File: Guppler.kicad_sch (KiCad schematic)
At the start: 21 parts, among them Q1 AO3400A, Q2 AO3400A, Q3 AO3400A, SW1 SW_Push, SW2 SW_Push, U1 LM2596S-3.3, U2 ESP32-C3-WROOM-02

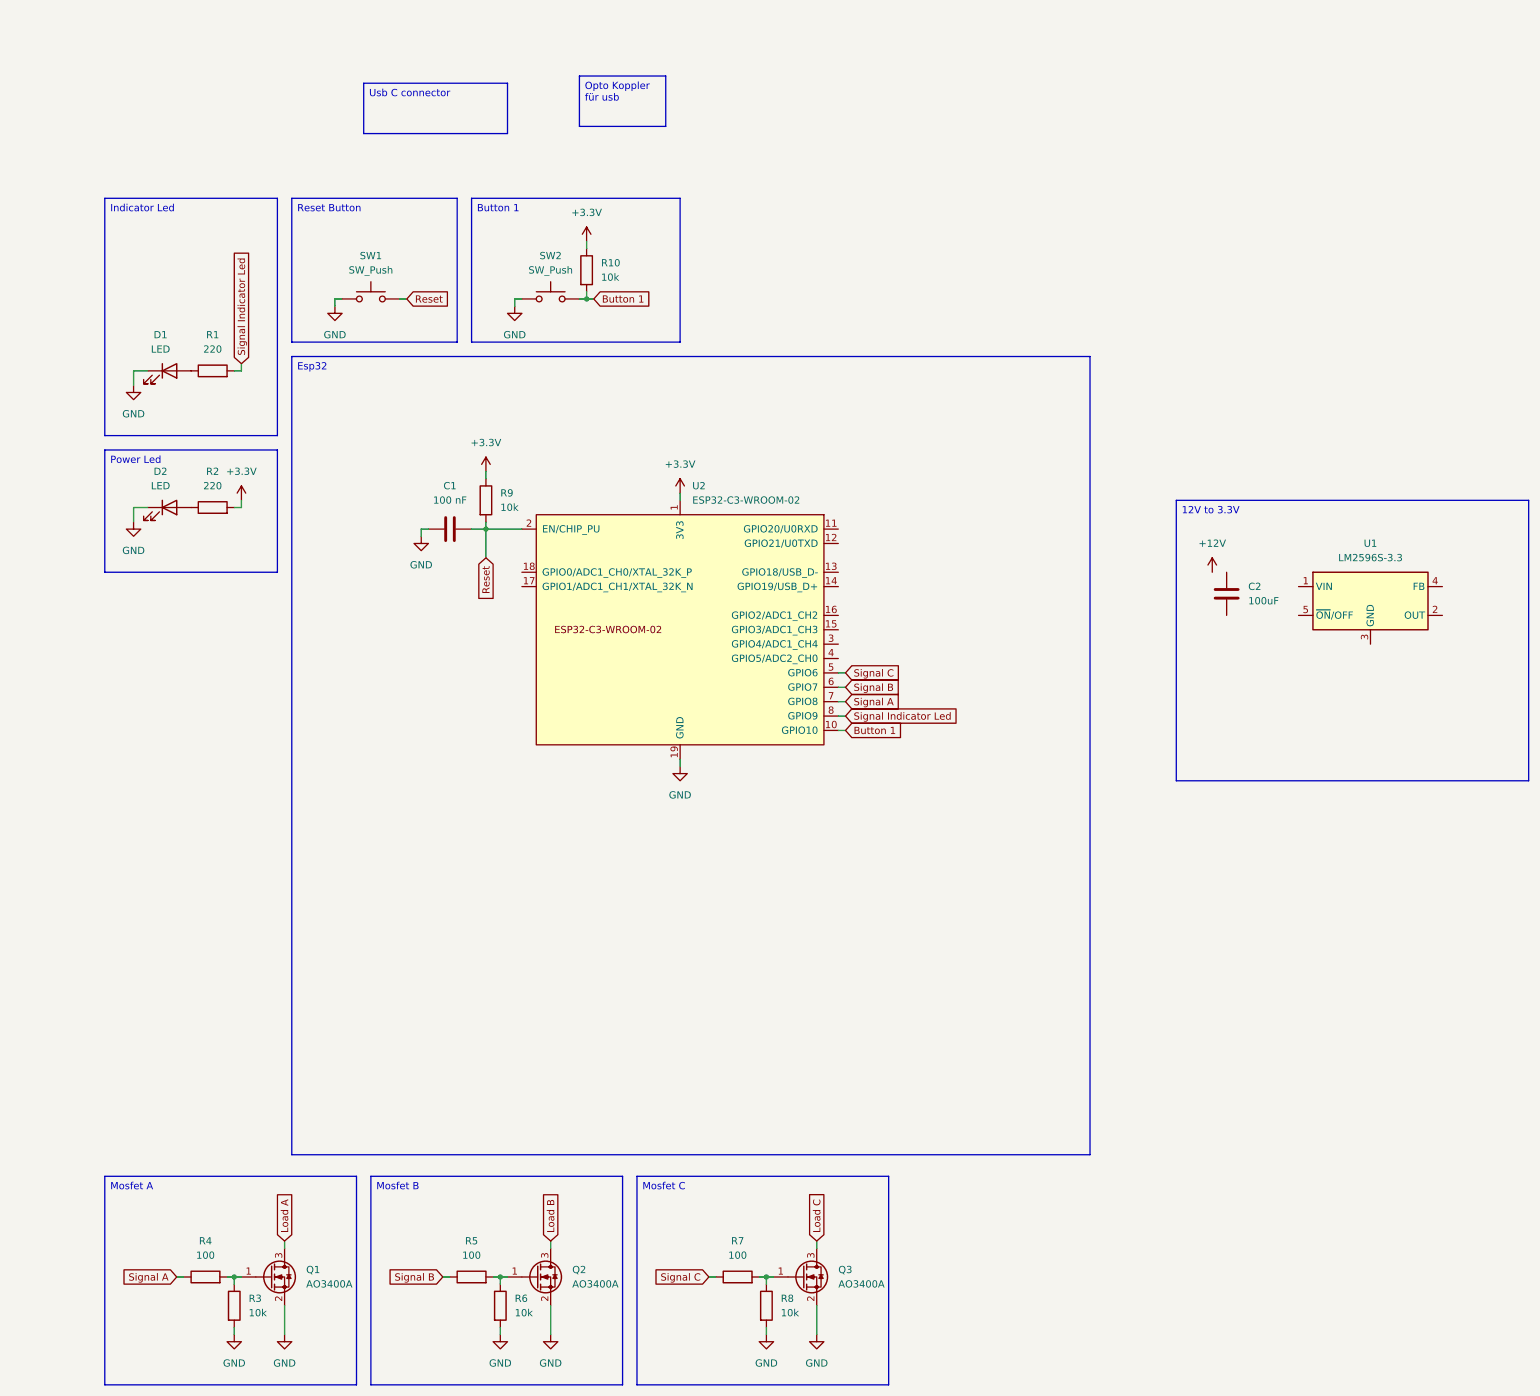
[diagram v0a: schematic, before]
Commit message: Add DC-DC Converter
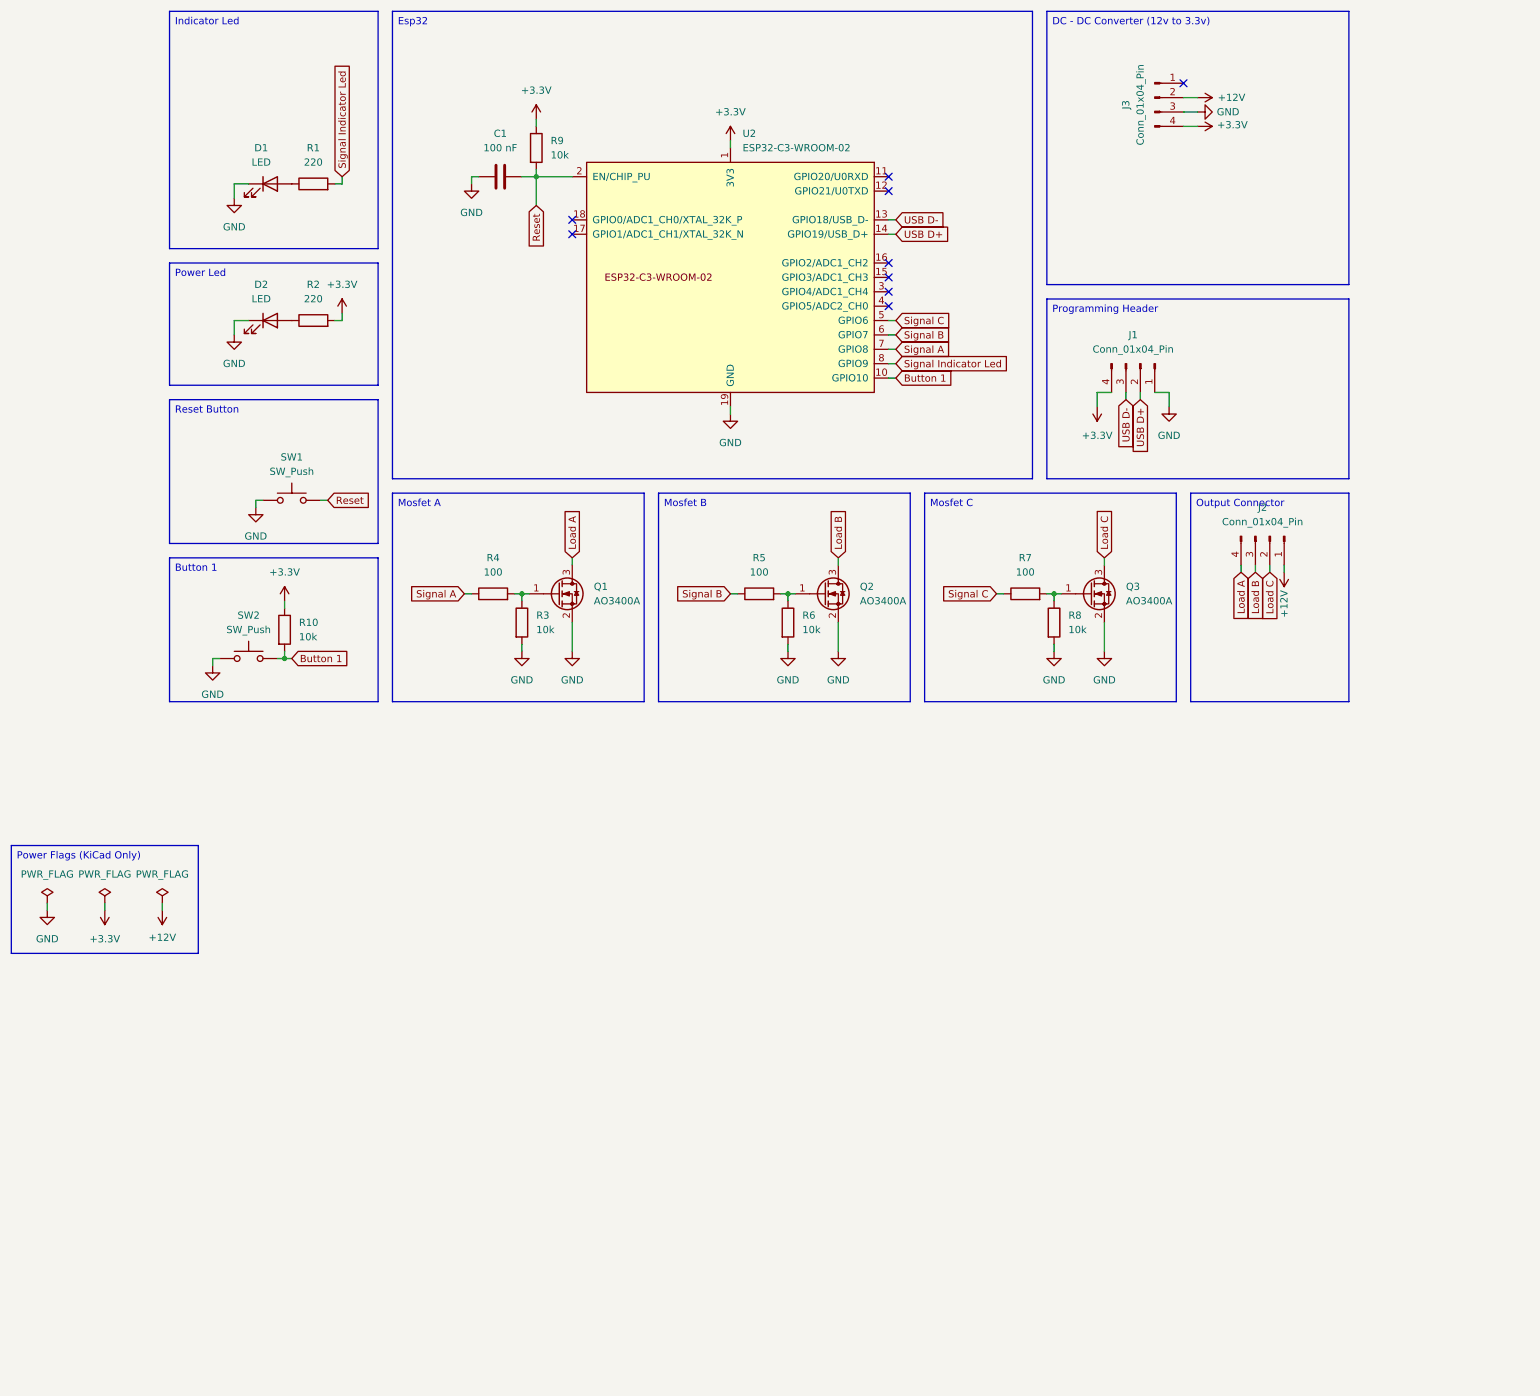
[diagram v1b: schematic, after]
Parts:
- removed C2: 100uF, symbol Device:C
- removed U1: LM2596S-3.3, Package_TO_SOT_SMD:TO-263-5_TabPin3, symbol Regulator_Switching:LM2596S-3.3
- added J1, J2, J3: Conn_01x04_Pin, symbol Connector:Conn_01x04_Pin
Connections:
- net +12V: now also J2.1 (Pin_1), J3.2 (Pin_2)
- net +3.3V: now also J1.4 (Pin_4), J3.4 (Pin_4)
- net GND: now also J1.1 (Pin_1), J3.3 (Pin_3)
- net Load A: now also J2.4 (Pin_4)
- net Load B: now also J2.3 (Pin_3)
- net Load C: now also J2.2 (Pin_2)
- net USB D-: now reaches U2.13 (GPIO18/USB_D-)
- net USB D-: now also J1.3 (Pin_3)
- net USB D+: now reaches U2.14 (GPIO19/USB_D+)
- net USB D+: now also J1.2 (Pin_2)
- no-connect marks 0 -> 9
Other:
- title: (none) -> Guppler Board
- moved on the sheet: C1, D1, D2, Q1, Q2, Q3, R1, R10, R2, R3, R4, R5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

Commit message: Create v0.1
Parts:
- removed J3: Conn_01x04_Pin, symbol Connector:Conn_01x04_Pin
- removed Q1, Q2, Q3: AO3400A, Package_TO_SOT_SMD:SOT-23, symbol Transistor_FET:AO3400A
- added J4: Conn_01x02_Pin, Connector_PinHeader_2.54mm:PinHeader_1x02_P2.54mm_Vertical, symbol Connector:Conn_01x02_Pin
- added LM2596_DC-DC1: 3.3V, Technogena:LM2596_DC-DC, symbol Techogena:LM2596_DC-DC
- added Q1, Q2, Q3: DMN2056U, Package_TO_SOT_SMD:SOT-23, symbol Transistor_FET:DMN2056U
- added R11, R12, R13: 10k, Resistor_SMD:R_0805_2012Metric_Pad1.20x1.40mm_HandSolder, symbol Device:R
- C1: footprint (none) -> Capacitor_SMD:C_0805_2012Metric_Pad1.18x1.45mm_HandSolder
- D1, D2: footprint (none) -> LED_SMD:LED_0805_2012Metric_Pad1.15x1.40mm_HandSolder
- J1, J2: footprint (none) -> Connector_PinHeader_2.54mm:PinHeader_1x04_P2.54mm_Vertical
- R1, R10, R2, R3, R4, R5, R6, R7, R8, R9: footprint (none) -> Resistor_SMD:R_0805_2012Metric_Pad1.20x1.40mm_HandSolder
- SW1, SW2: footprint (none) -> Button_Switch_THT:SW_PUSH_6mm_H5mm
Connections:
- net +12V: now also LM2596_DC-DC1.1 (OUT+)
- net +3.3V: now also LM2596_DC-DC1.0 (IN+), R11.2, R12.2, R13.2
- net GND: now also J4.2 (Pin_2), LM2596_DC-DC1.2 (OUT-), LM2596_DC-DC1.3 (IN-), Q1.2 (S), Q2.2 (S), Q3.2 (S)
- net Load A: now also Q2.3 (D)
- net Load B: now also Q1.3 (D)
- net Load C: now also Q3.3 (D)
- net Signal A: now also U2.5 (GPIO6); no longer U2.7 (GPIO8)
- net Signal C: now also U2.3 (GPIO4/ADC1_CH4); no longer U2.5 (GPIO6)
- net Signal Indicator Led: now also U2.4 (GPIO5/ADC2_CH0); no longer U2.8 (GPIO9)
- net at R7.2, R8.1: now also Q3.1 (G)
- net at R5.2, R6.1: now also Q1.1 (G)
- net at R3.1, R4.2: now also Q2.1 (G)
- net at U2.16 (GPIO2/ADC1_CH2): now also R12.1
- new net: J4.1 (Pin_1), R11.1, U2.8 (GPIO9)
- new net: R13.1, U2.7 (GPIO8)
- no-connect marks 9 -> 5
